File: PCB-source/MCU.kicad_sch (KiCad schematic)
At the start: 39 parts, among them U403 STM32H562VGTx, X300 Q13FC1350000400, Y400 ASE-xxxMHz

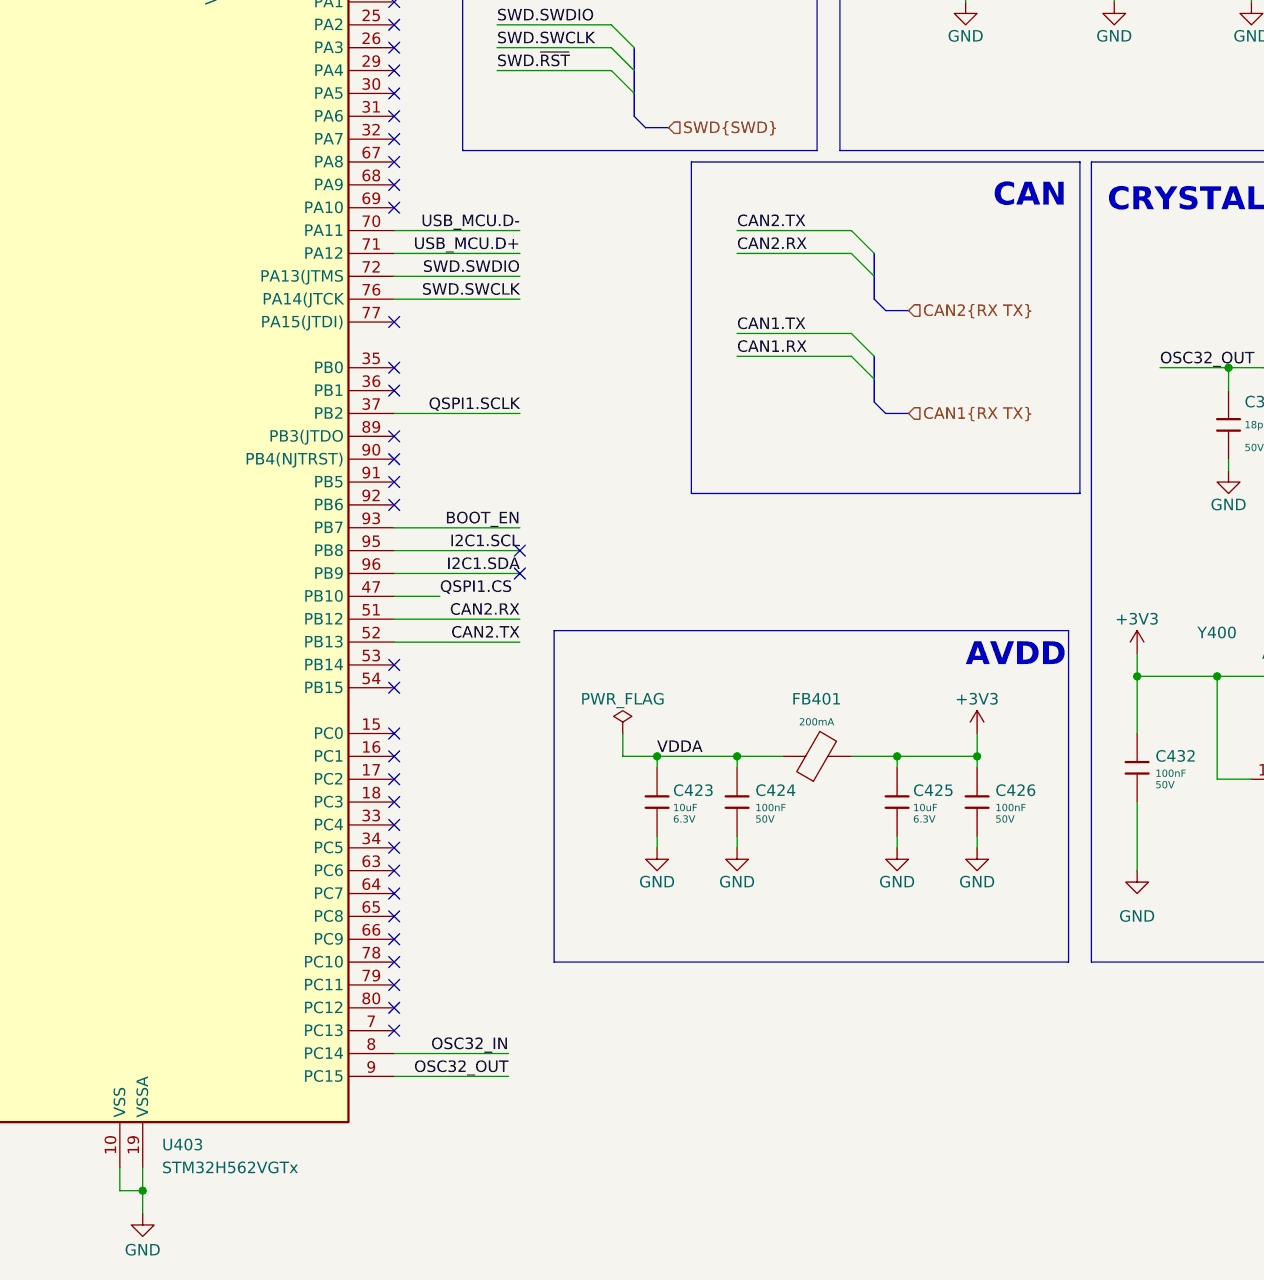
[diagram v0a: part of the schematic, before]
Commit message: Finish component and diffpair placement
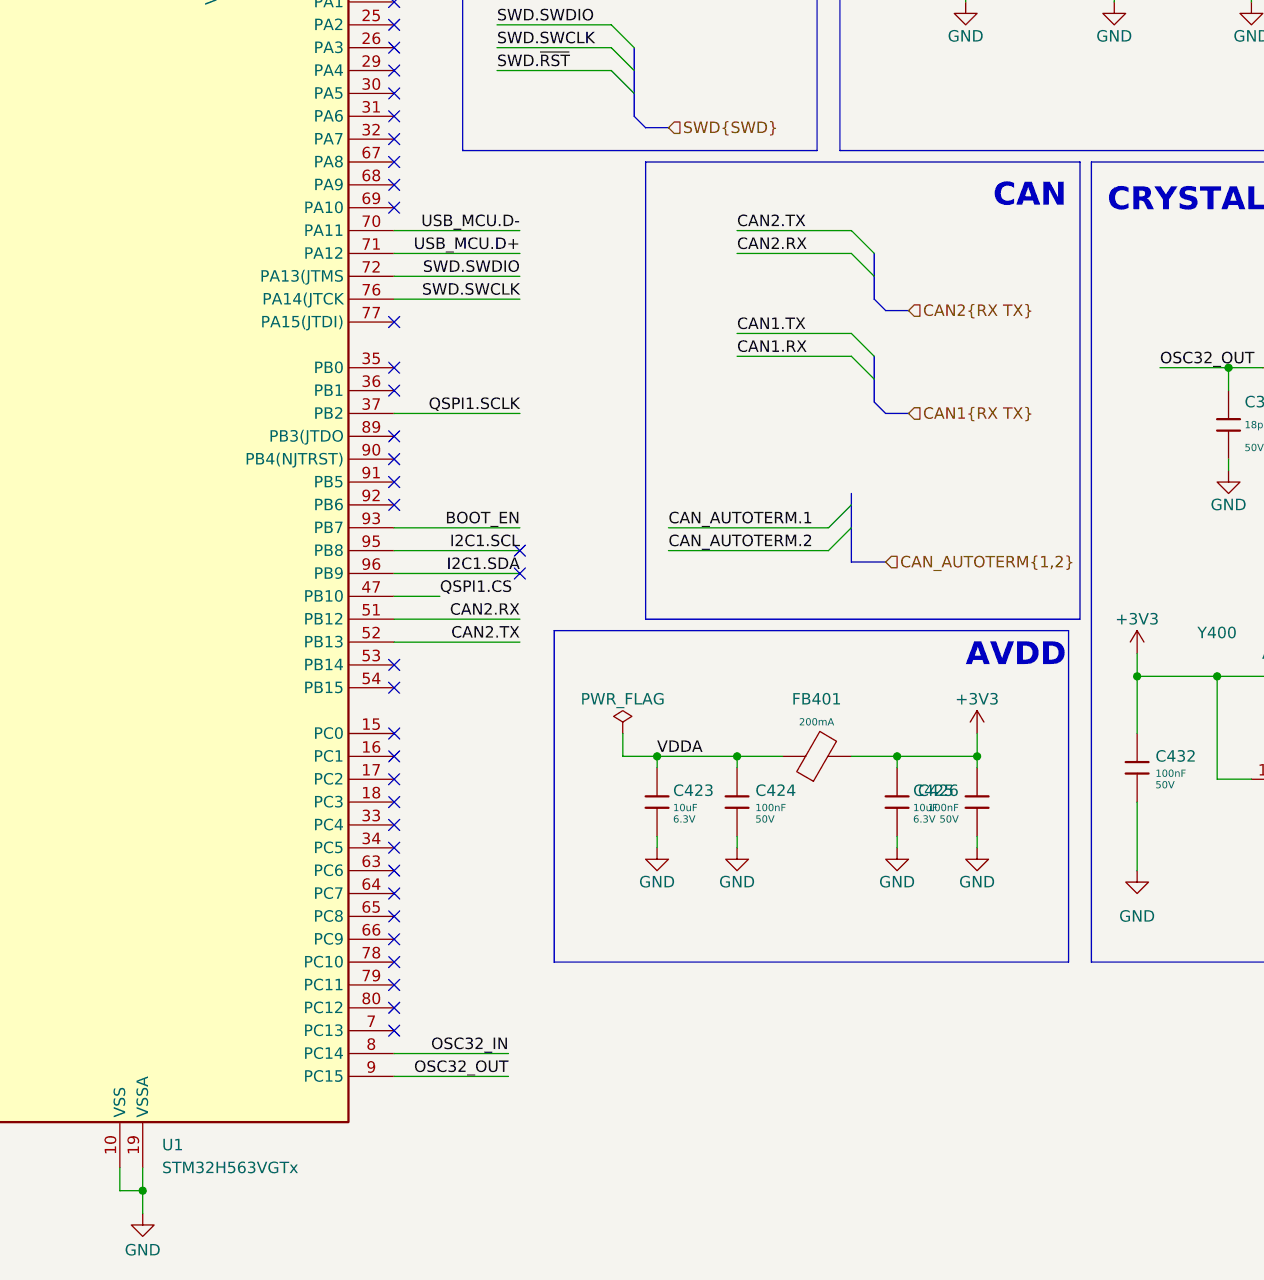
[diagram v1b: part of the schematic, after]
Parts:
- removed U403: STM32H562VGTx, Package_QFP:LQFP-100_14x14mm_P0.5mm, symbol MCU_ST_STM32H5:STM32H562VGTx
- added U1: STM32H563VGTx, Package_QFP:LQFP-100_14x14mm_P0.5mm, symbol MCU_ST_STM32H5:STM32H563VGTx
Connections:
- net +3V3: now also U1.100 (VDD), U1.11 (VDD), U1.21 (VREF+), U1.28 (VDD), U1.50 (VDD), U1.6 (VBAT), U1.73 (VDDUSB), U1.75 (VDD)
- net BOOT0: now also U1.94 (BOOT0)
- net BOOT_EN: now also U1.93 (PB7)
- net CAN1.RX: now also U1.81 (PD0)
- net CAN1.TX: now also U1.82 (PD1)
- net CAN2.RX: now also U1.51 (PB12)
- net CAN2.TX: now also U1.52 (PB13)
- net GND: now also U1.10 (VSS), U1.19 (VSSA), U1.20 (VREF-), U1.27 (VSS), U1.49 (VSS), U1.74 (VSS), U1.99 (VSS)
- net I2C1.SCL: now also U1.95 (PB8)
- net I2C1.SDA: now also U1.96 (PB9)
- net OSC32_IN: now also U1.8 (PC14)
- net OSC32_OUT: now also U1.9 (PC15)
- net OSC_IN: now also U1.12 (PH0)
- net QSPI1.CS: now also U1.47 (PB10)
- net QSPI1.IO0: now also U1.58 (PD11)
- net QSPI1.IO1: now also U1.59 (PD12)
- net QSPI1.IO2: now also U1.1 (PE2)
- net QSPI1.IO3: now also U1.60 (PD13)
- net QSPI1.SCLK: now also U1.37 (PB2)
- net STATUS_LED: now also U1.4 (PE5)
- net SWD.SWCLK: now also U1.76 (PA14(JTCK)
- net SWD.SWDIO: now also U1.72 (PA13(JTMS)
- net SWD.~{RST}: now also U1.14 (NRST)
- net USB_MCU.D+: now also U1.71 (PA12)
- net USB_MCU.D-: now also U1.70 (PA11)
- net USER_LED_1: now also U1.2 (PE3)
- net USER_LED_2: now also U1.3 (PE4)
- net USR_BUTTON: now also U1.5 (PE6)
- net VCAP_1: now also U1.48 (VCAP)
- net VCAP_2: now also U1.98 (VCAP)
- net VDDA: now also U1.22 (VDDA)

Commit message: in progress
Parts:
- removed LED300, LED301: FixLed307, FixLed307:FixLed307, symbol FixLed307:FixLed307
